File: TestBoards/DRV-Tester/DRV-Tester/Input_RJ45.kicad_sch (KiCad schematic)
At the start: 1 part, among them U4 XT30PW-F

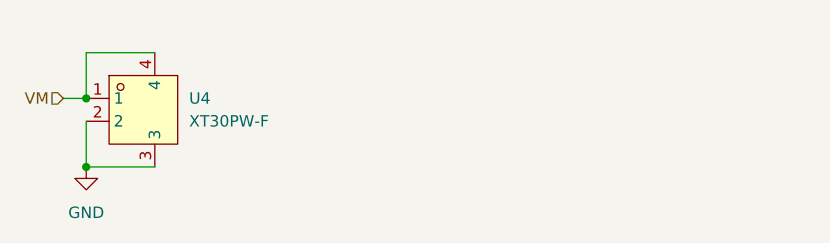
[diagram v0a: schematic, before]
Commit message: update tester board with layout
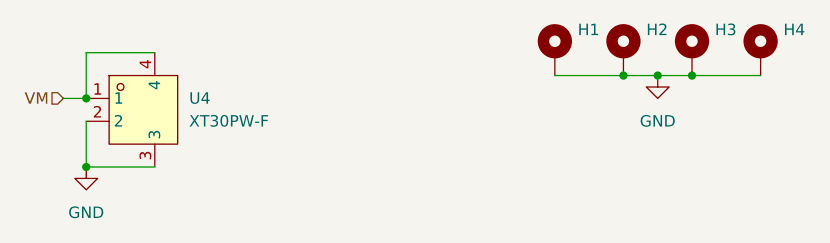
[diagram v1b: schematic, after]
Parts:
- added H1, H2, H3, H4: MountingHole_Pad, MountingHole:MountingHole_3.2mm_M3, symbol Mechanical:MountingHole_Pad
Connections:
- net GND: now also H1.1, H2.1, H3.1, H4.1
